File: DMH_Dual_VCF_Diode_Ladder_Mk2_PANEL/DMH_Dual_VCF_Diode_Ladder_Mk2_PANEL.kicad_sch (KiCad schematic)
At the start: 45 parts, among them J0 Panel_GND_Solder_Wire_Pad

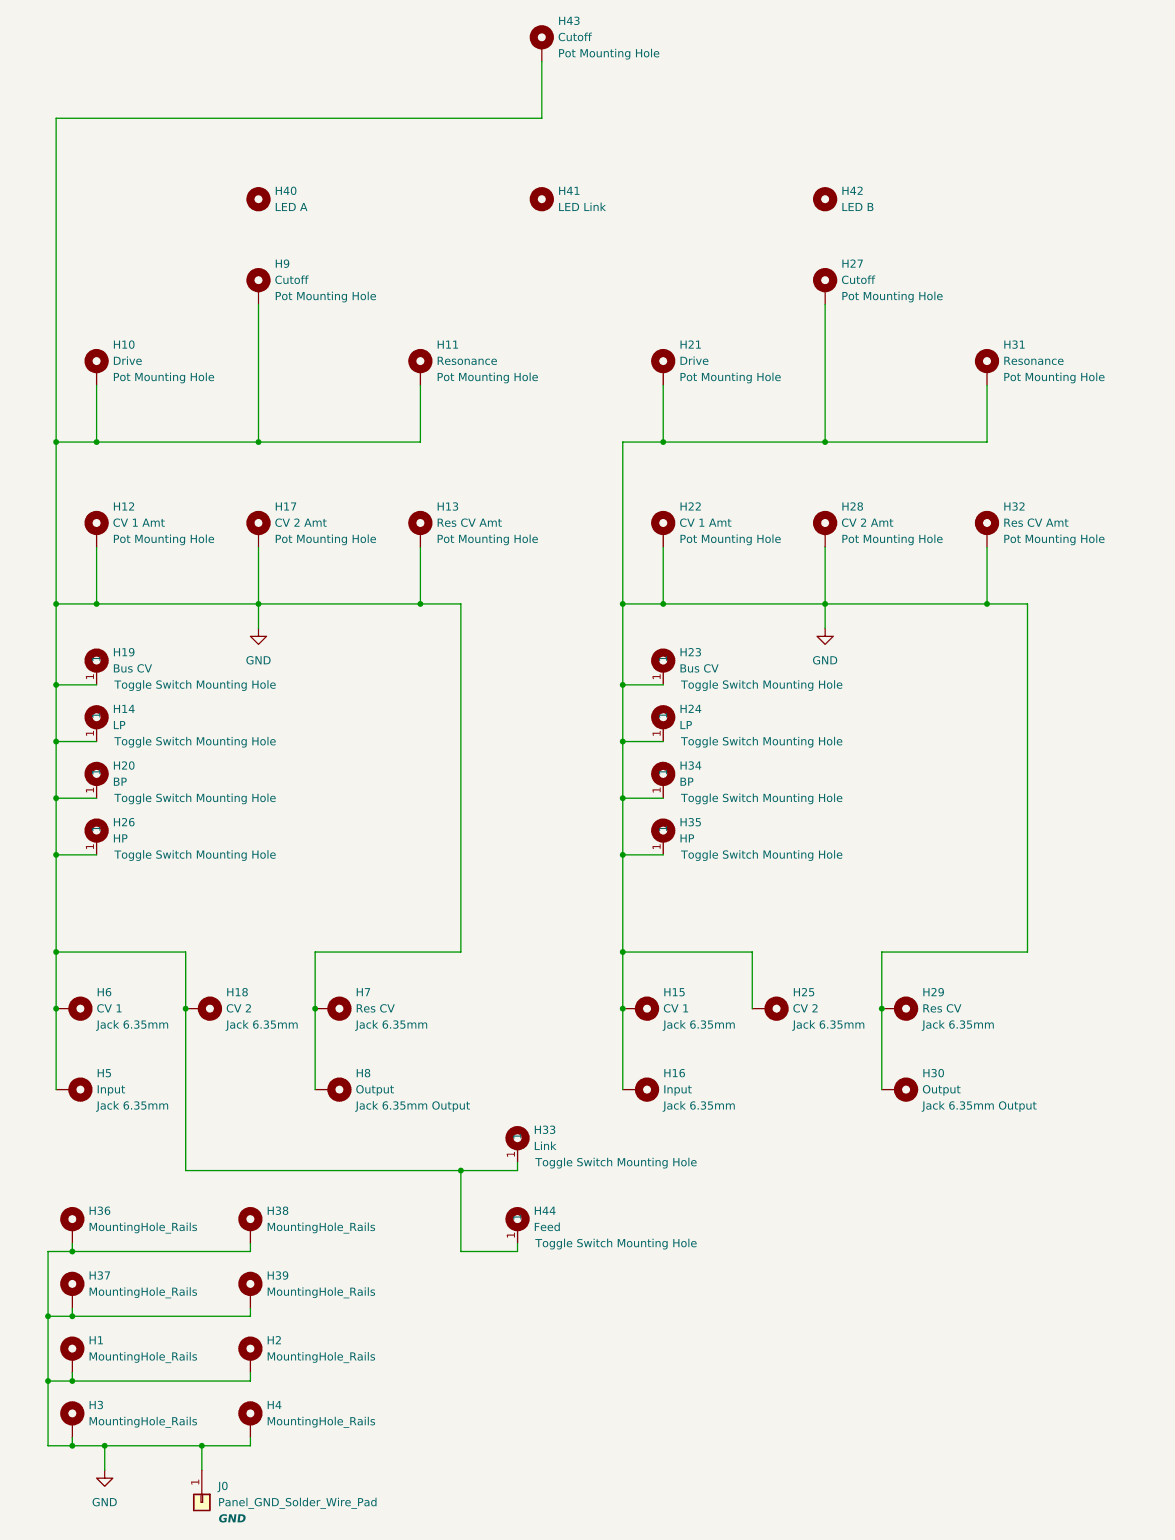
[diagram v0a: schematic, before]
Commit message: Added CV3 and Drive CV to Panel
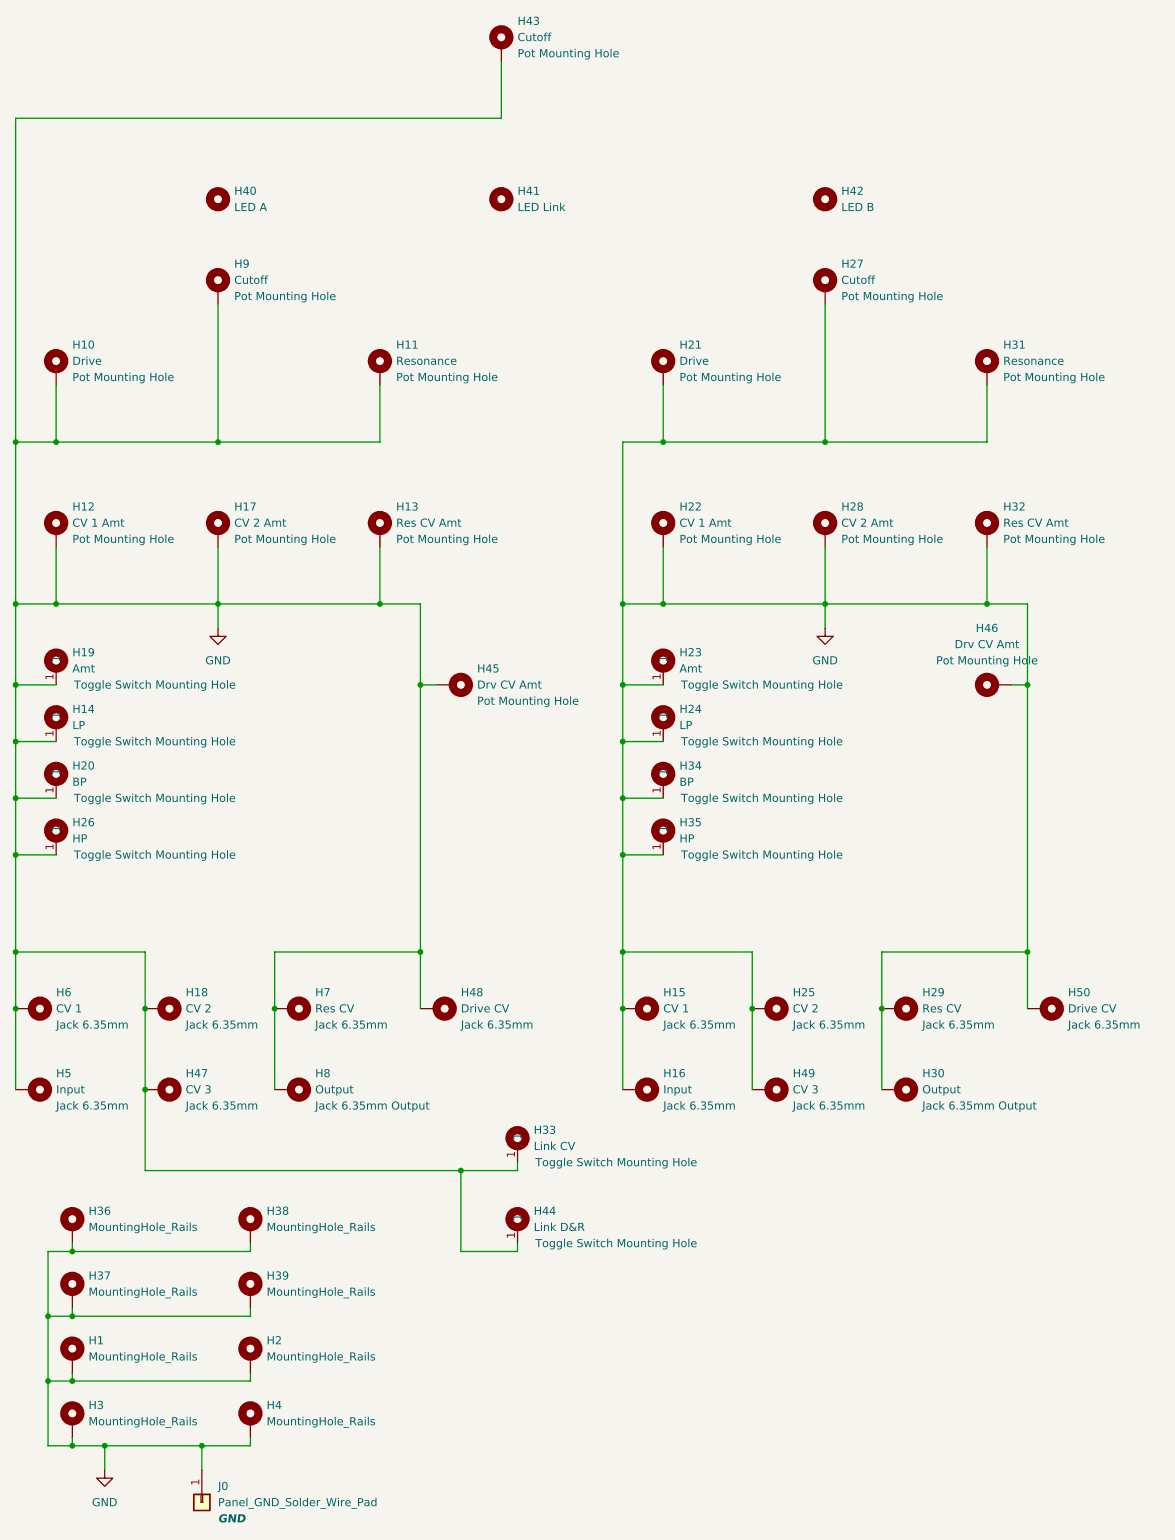
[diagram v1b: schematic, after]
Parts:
- added H45, H46: Drv CV Amt, SynthStuff:Pot_Cutout_Tiny_attv_P110KH1, symbol SynthStuff:MountingHole_Pot
- added H47, H49: CV 3, SynthStuff:Jack_6.35mm_Cutout_v3, symbol SynthStuff:MountingHole_Jack6.35mm_v2
- added H48, H50: Drive CV, SynthStuff:Jack_6.35mm_Cutout_v3, symbol SynthStuff:MountingHole_Jack6.35mm_v2
- H19, H23: value Bus CV -> Amt
- H33: value Link -> Link CV
- H44: value Feed -> Link D&R
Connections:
- net GND: now also H45.1, H46.1, H47.1, H48.1, H49.1, H50.1
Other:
- moved on the sheet: H10, H11, H12, H13, H14, H17, H18, H19, H20, H26, H40, H41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

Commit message: Moved Res Int and CV3 V/Oct trims to front panel
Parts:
- added H51, H52: Res Int, SynthStuff:MountingHole_TrimPot, symbol SynthStuff:MountingHole_Trimpot
- added H53, H54: CV3 V/Oct, SynthStuff:MountingHole_TrimPot, symbol SynthStuff:MountingHole_Trimpot

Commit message: KiCad 9.0.7 + centralized library
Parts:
- H40, H42: footprint SynthStuff:MountingHole_LED_3mm -> SynthStuff:MountingHole_LED_3mm_R
- H41: footprint SynthStuff:MountingHole_LED_3mm -> SynthStuff:MountingHole_LED_3mm_B
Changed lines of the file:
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@@
 			)
 		)
-		(property "Footprint" "SynthStuff:MountingHole_LED_3mm"
+		(property "Footprint" "SynthStuff:MountingHole_LED_3mm_R"
 			(at 146.05 76.2 0)
 			(effects
@@
 			)
 		)
-		(property "Footprint" "SynthStuff:MountingHole_LED_3mm"
+		(property "Footprint" "SynthStuff:MountingHole_LED_3mm_B"
 			(at 95.25 76.2 0)
 			(effects
@@
 			)
 		)
-		(property "Footprint" "SynthStuff:MountingHole_LED_3mm"
+		(property "Footprint" "SynthStuff:MountingHole_LED_3mm_R"
 			(at 50.8 76.2 0)
 			(effects
